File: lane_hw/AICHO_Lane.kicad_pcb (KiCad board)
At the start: 2 copper layers, 64 parts, among them J1 JST PH, J2 RJ45, J41 JST PH, J42 JST PH, J43 JST PH, J9 Conn_01x04, Q41 AO3400A, Q42 AO3400A, Q43 AO3400A, U1 TPS54302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

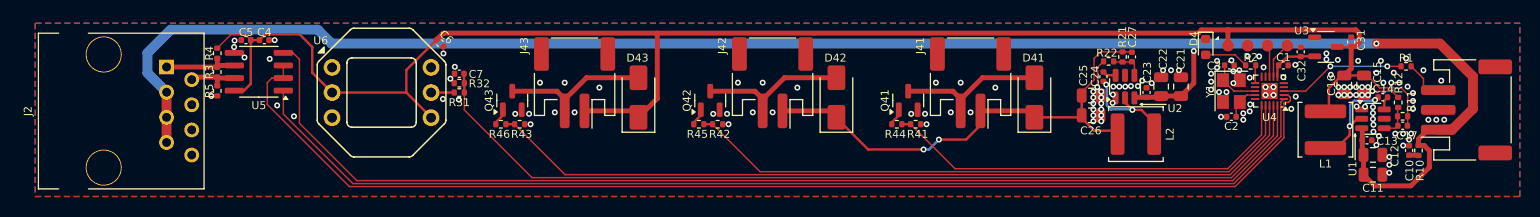
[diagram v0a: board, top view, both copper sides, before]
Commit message: lane_hw: Add bulk capacitors and mounting holes
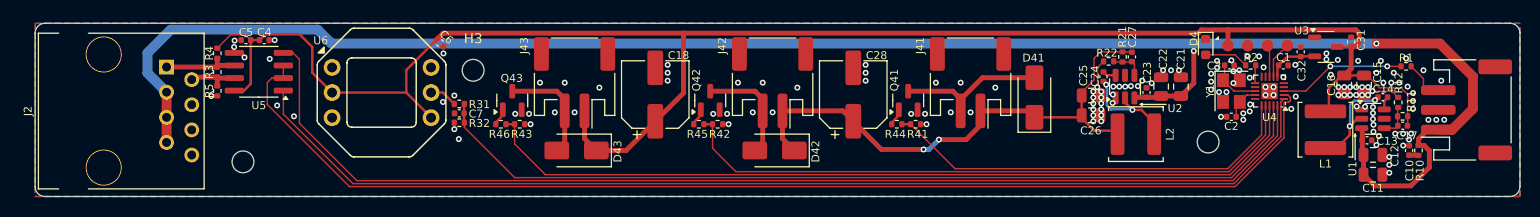
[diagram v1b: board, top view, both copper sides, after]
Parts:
- added C18: 220u 25V, Capacitor_SMD:CP_Elec_6.3x7.7, F.Cu at (113.2, 47.2)
- added C28: 220u 25V, Capacitor_SMD:CP_Elec_6.3x7.7, F.Cu at (133.2, 47.2)
- added H1: MountingHole, MountingHole:MountingHole_2.2mm_M2, F.Cu at (71.5, 54.0)
- added H2: MountingHole, MountingHole:MountingHole_2.2mm_M2, F.Cu at (169.0, 52.0)
- added H3: MountingHole, MountingHole:MountingHole_2.2mm_M2, F.Cu at (94.8, 44.8)
- moved D43 8.23 mm to (105.2, 52.9), turned to 180 degrees
- moved D42 8.23 mm to (125.2, 52.9), turned to 180 degrees
- moved C7 4.00 mm to (93.3, 49.1)
- moved R32 4.00 mm to (93.3, 50.0)
- moved R31 1.15 mm to (93.3, 48.1)
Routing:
- net +5V: track 172.2 -> 179.0 mm
- net +12V: track 49.2 -> 53.7 mm
- net Net-(D43-A): track 15.2 -> 11.2 mm
- net Net-(D42-A): track 15.2 -> 11.2 mm
- net /PRESSURE_SENSOR: track 93.1 -> 91.0 mm
- net /PUMP_2: track 63.3 -> 64.7 mm
- net /PUMP_3: track 83.9 -> 85.1 mm
- net GND: vias 141 -> 147
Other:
- board outline added: 150 x 17.5 mm

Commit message: lane_hw: Finalize routing & vias
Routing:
- net GND: vias 147 -> 277
- added copper zone on F.Cu, net +5V

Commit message: lane_hw: Finalize, again
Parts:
- added G***: LOGO, LOGO, F.Cu at (148.5, 54.8)
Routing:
- net GND: vias 277 -> 295
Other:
- board text added: "<25-"
- board text added: ">"
- board text added: "AICHO"
- board text added: "Rev. 3"
- board text added: "ayu.land/aicho?id=L3_xx"
- board text added: "寒露"

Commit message: lane_hw: Modify attributes per fabrication settings
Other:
- board text added: "ayu.land/aicho?id=R3_Lxx"
- board text removed: "ayu.land/aicho?id=L3_xx"
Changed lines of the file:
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@@
 			)
 		)
-		(property "LCSC PN" "C51940124"
+		(property "LCSC PN" "C7433648"
 			(at 0 0 180)
 			(unlocked yes)
@@
 			)
 		)
-		(property "LCSC PN" "C51940124"
+		(property "LCSC PN" "C7433648"
 			(at 0 0 180)
 			(unlocked yes)
@@
 			)
 		)
-		(property "LCSC PN" "C51940124"
+		(property "LCSC PN" "C7433648"
 			(at 0 0 180)
 			(unlocked yes)
@@
 		)
 	)
-	(gr_text "ayu.land/aicho?id=L3_xx"
+	(gr_text "ayu.land/aicho?id=R3_Lxx"
 		(at 74.5 58.5 0)
 		(layer "Cmts.User")

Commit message: lane_hw: Revise silkscreen
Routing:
- net GND: vias 295 -> 296
